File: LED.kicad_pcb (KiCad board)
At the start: 2 copper layers, 235 x 18 mm, 8 parts

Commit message: working for free
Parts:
- added C1: 2.2u, 3rdparty:CAPC2012X140N, F.Cu at (165.0, 96.2)
- added C5: 0.1u, 3rdparty:CAPC2012X140N, F.Cu at (165.0, 99.0)
- added C6: 1.5n, 3rdparty:CAPC2012X140N, F.Cu at (165.0, 101.8)
- added COUT1: 10u, 3rdparty:CAPC2012X140N, F.Cu at (165.0, 104.6)
- added D1: D, Package_TO_SOT_SMD:TO-252-2, F.Cu at (137.0, 92.7)
- added D2: D, Package_TO_SOT_SMD:TO-252-2, F.Cu at (153.5, 92.7)
- added IC1: MAX25603AUI_V+, 3rdparty:SOP65P640X110-29N, F.Cu at (192.5, 91.5)
- added Q1: FDMC8032L, Package_SON:Fairchild_DualPower33-6_3x3mm, F.Cu at (175.4, 90.5)
- added Q2: FDMC8032L, Package_SON:Fairchild_DualPower33-6_3x3mm, F.Cu at (169.6, 102.0)
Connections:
- LED4 pad 2: Net-(LED4-A_1) -> Net-(IC1-ISN)
- LED4 pad 4: Net-(LED4-A_1) -> Net-(IC1-ISN)
- LED5 pad 1: Net-(LED1-K_1) -> GND
- LED5 pad 3: Net-(LED1-K_1) -> GND
- LED8 pad 2: Net-(LED4-A_1) -> Net-(LED1-K_1)
- LED8 pad 4: Net-(LED4-A_1) -> Net-(LED1-K_1)

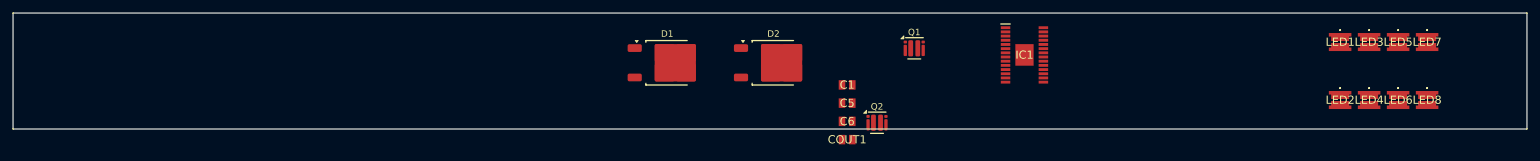
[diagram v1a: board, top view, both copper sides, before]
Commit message: placed leds
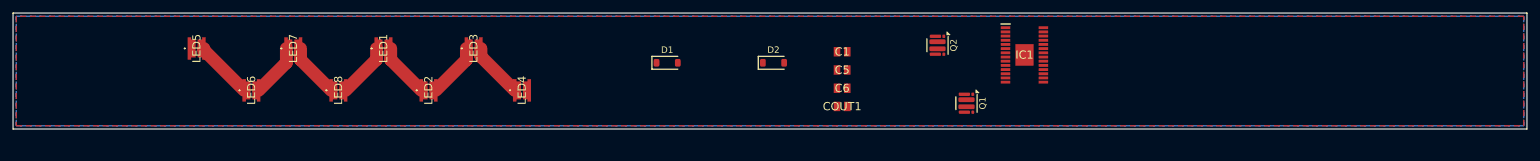
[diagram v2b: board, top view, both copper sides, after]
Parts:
- D1, D2: footprint Package_TO_SOT_SMD:TO-252-2 -> Diode_SMD:D_SOD-123
- moved LED5 186.5 mm to (64.0, 90.5), turned to 90 degrees
- moved LED6 178.0 mm to (72.5, 97.0), turned to 90 degrees
- moved LED7 176.0 mm to (79.0, 90.5), turned to 90 degrees
- moved LED8 169.0 mm to (86.0, 97.0), turned to 90 degrees
- moved LED1 148.5 mm to (93.0, 90.5), turned to 90 degrees
- moved LED2 141.5 mm to (100.0, 97.0), turned to 90 degrees
- moved LED3 139.0 mm to (107.0, 90.5), turned to 90 degrees
- moved LED4 131.5 mm to (114.5, 97.0), turned to 90 degrees
- moved Q2 15.3 mm to (179.0, 90.0), turned to -90 degrees
- moved Q1 11.8 mm to (183.5, 99.0), turned to -90 degrees
- moved C1 5.20 mm to (164.2, 91.0)
- moved C5 5.20 mm to (164.2, 93.8)
- moved C6 5.20 mm to (164.2, 96.7)
- moved COUT1 5.20 mm to (164.2, 99.5)
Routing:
- net Net-(LED5-A_1): track 0.00 -> 9.09 mm
- net Net-(LED3-A_1): track 0.00 -> 8.67 mm
- net Net-(LED1-K_1): track 0.00 -> 8.49 mm
- net Net-(LED7-A_1): track 0.00 -> 8.47 mm
- net Net-(LED2-A_1): track 0.00 -> 8.47 mm
- net Net-(LED1-A_1): track 0.00 -> 8.47 mm
- net Net-(LED6-A_1): track 0.00 -> 8.28 mm
- added copper zone on B.Cu, net GND
- added copper zone on F.Cu, net GND

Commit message: more free work (done pcb)
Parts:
- added C2: 0.1u, Capacitor_SMD:CAPC2012X140N, F.Cu at (207.4, 96.3)
- added C3: 0.1u, Capacitor_SMD:CAPC2012X140N, F.Cu at (215.4, 90.9)
- added C4: 1u, Capacitor_SMD:CAPC2012X140N, F.Cu at (256.2, 89.4)
- added J1: Barrel_Jack, Connector_BarrelJack:BarrelJack_Horizontal, F.Cu at (261.4, 92.4)
- added L1: 20u, Inductor_SMD_Wurth:7843332000, F.Cu at (245.8, 94.0)
- added R1: 0.02, Resistor_SMD:R_0805_2012Metric, F.Cu at (213.5, 99.4)
- added R2: 1.27k, Resistor_SMD:R_0805_2012Metric, F.Cu at (215.5, 99.4)
- added R3: 0.02, Resistor_SMD:R_0805_2012Metric, F.Cu at (211.5, 99.4)
- added R4: 100, Resistor_SMD:R_0805_2012Metric, F.Cu at (226.3, 96.0)
- added R5: 100k, Resistor_SMD:R_0805_2012Metric, F.Cu at (223.4, 88.2)
- added RDL1: 10k, Resistor_SMD:R_0805_2012Metric, F.Cu at (209.6, 99.4)
- added RDL2: 10k, Resistor_SMD:R_0805_2012Metric, F.Cu at (237.3, 89.3)
- added RLED1: 2, Resistor_SMD:R_0805_2012Metric, F.Cu at (177.2, 97.4)
- added RLED2: 2, Resistor_SMD:R_0805_2012Metric, F.Cu at (175.2, 97.4)
- added RV1: 10k, Potentiometer_SMD:Potentiometer_Vishay_TS53YJ_Vertical, F.Cu at (228.6, 90.0)
- IC1: footprint 3rdparty:SOP65P640X110-29N -> LED_SMD:SOP65P640X110-29N
- LED1, LED2, LED3, LED4, LED5, LED6, LED7, LED8: footprint 3rdparty:SPMWHD32AMH0XAR0PR -> LED_SMD:SPMWHD32AMH0XAR0PR
- moved Q2 75.9 mm to (254.8, 93.8)
- moved D1 67.6 mm to (204.4, 97.7), turned to -90 degrees
- moved C6 64.1 mm to (228.3, 96.0), turned to -90 degrees
- moved C5 62.7 mm to (226.7, 98.6)
- moved D2 61.9 mm to (215.2, 88.1), turned to 180 degrees
- moved Q1 53.8 mm to (237.1, 93.7)
- moved LED1 52.8 mm to (145.8, 90.3)
- moved LED2 52.8 mm to (152.8, 96.8)
- moved LED3 52.8 mm to (159.8, 90.3)
- moved LED4 52.8 mm to (167.3, 96.8)
- moved LED5 52.8 mm to (116.8, 90.3)
- moved LED6 52.8 mm to (125.3, 96.8)
- moved LED7 52.8 mm to (131.8, 90.3)
- moved LED8 52.8 mm to (138.8, 96.8)
- moved C1 44.2 mm to (207.6, 99.7), turned to -90 degrees
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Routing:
- net Net-(IC1-LX1): track 0.00 -> 105.3 mm
- net +24V: track 0.00 -> 76.9 mm, vias 0 -> 6
- net Net-(IC1-ISN): track 0.00 -> 64.6 mm, vias 0 -> 2
- net Net-(IC1-LX2): track 0.00 -> 58.3 mm, vias 0 -> 4
- net Net-(IC1-DL1): track 0.00 -> 55.0 mm, vias 0 -> 3
- net +12V: track 0.00 -> 52.4 mm
- net Net-(D1-A): track 0.00 -> 50.1 mm
- net Net-(IC1-DH1): track 0.00 -> 49.2 mm, vias 0 -> 4
- net Net-(Q1B-S2): track 0.00 -> 48.3 mm, vias 0 -> 2
- net Net-(IC1-DL2): track 0.00 -> 45.4 mm, vias 0 -> 2
- net Net-(IC1-DH2): track 0.00 -> 33.3 mm, vias 0 -> 2
- net GND: track 0.00 -> 24.4 mm, vias 0 -> 21
- net Net-(D1-K): track 0.00 -> 17.7 mm, vias 0 -> 2
- net Net-(IC1-ICTRL): track 0.00 -> 12.2 mm
- net Net-(D2-K): track 0.00 -> 7.61 mm
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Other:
- board size 235 x 18 mm -> 159.8 x 18 mm

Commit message: bed
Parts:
- added C7: 68uF, Capacitor_SMD:CP_Elec_6.3x5.4, F.Cu at (261.0, 97.7)
- C4: value 1u -> 1uF
- COUT1: footprint 3rdparty:CAPC2012X140N -> Capacitor_SMD:C_1206_3216Metric
- J1: value Barrel_Jack -> Screw_Terminal_01x02; footprint Connector_BarrelJack:BarrelJack_Horizontal -> TerminalBlock_MetzConnect:TerminalBlock_MetzConnect_Type086_RT03402HBLC_1x02_P3.81mm_Horizontal
- R1, R3: footprint Resistor_SMD:R_0805_2012Metric -> Resistor_SMD:R_1210_3225Metric
- moved R1 15.9 mm to (197.7, 97.6)
- moved R3 10.5 mm to (201.2, 97.5)
- moved J1 6.56 mm to (265.9, 87.6), turned to -90 degrees
- moved COUT1 0.72 mm to (179.7, 96.8)
- moved C1 0.06 mm to (207.6, 99.6)
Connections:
- J1 pad 1: +12V -> GND
- J1 pad 2: GND -> +12V
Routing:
- net Net-(IC1-LX1): track 105.3 -> 27.8 mm
- net Net-(Q1B-S2): track 48.3 -> 62.2 mm
- net +12V: track 52.4 -> 63.1 mm
- net Net-(IC1-DL1): track 55.0 -> 47.5 mm
- net Net-(IC1-LX2): track 58.3 -> 56.7 mm
- net GND: track 24.4 -> 23.5 mm, vias 21 -> 19
- net Net-(IC1-DL2): track 45.4 -> 44.7 mm
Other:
- board size 159.8 x 18 mm -> 159.8 x 18.2 mm
